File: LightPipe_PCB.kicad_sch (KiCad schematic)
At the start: 12 parts, among them X1 Lumberg KLB4, X2 Lumberg KLB4, X3 XT30, X4.1 Cable-0.7mm, X4.2 Cable-0.7mm, X5.1 Cable-1.5mm, X5.2 Cable-1.5mm

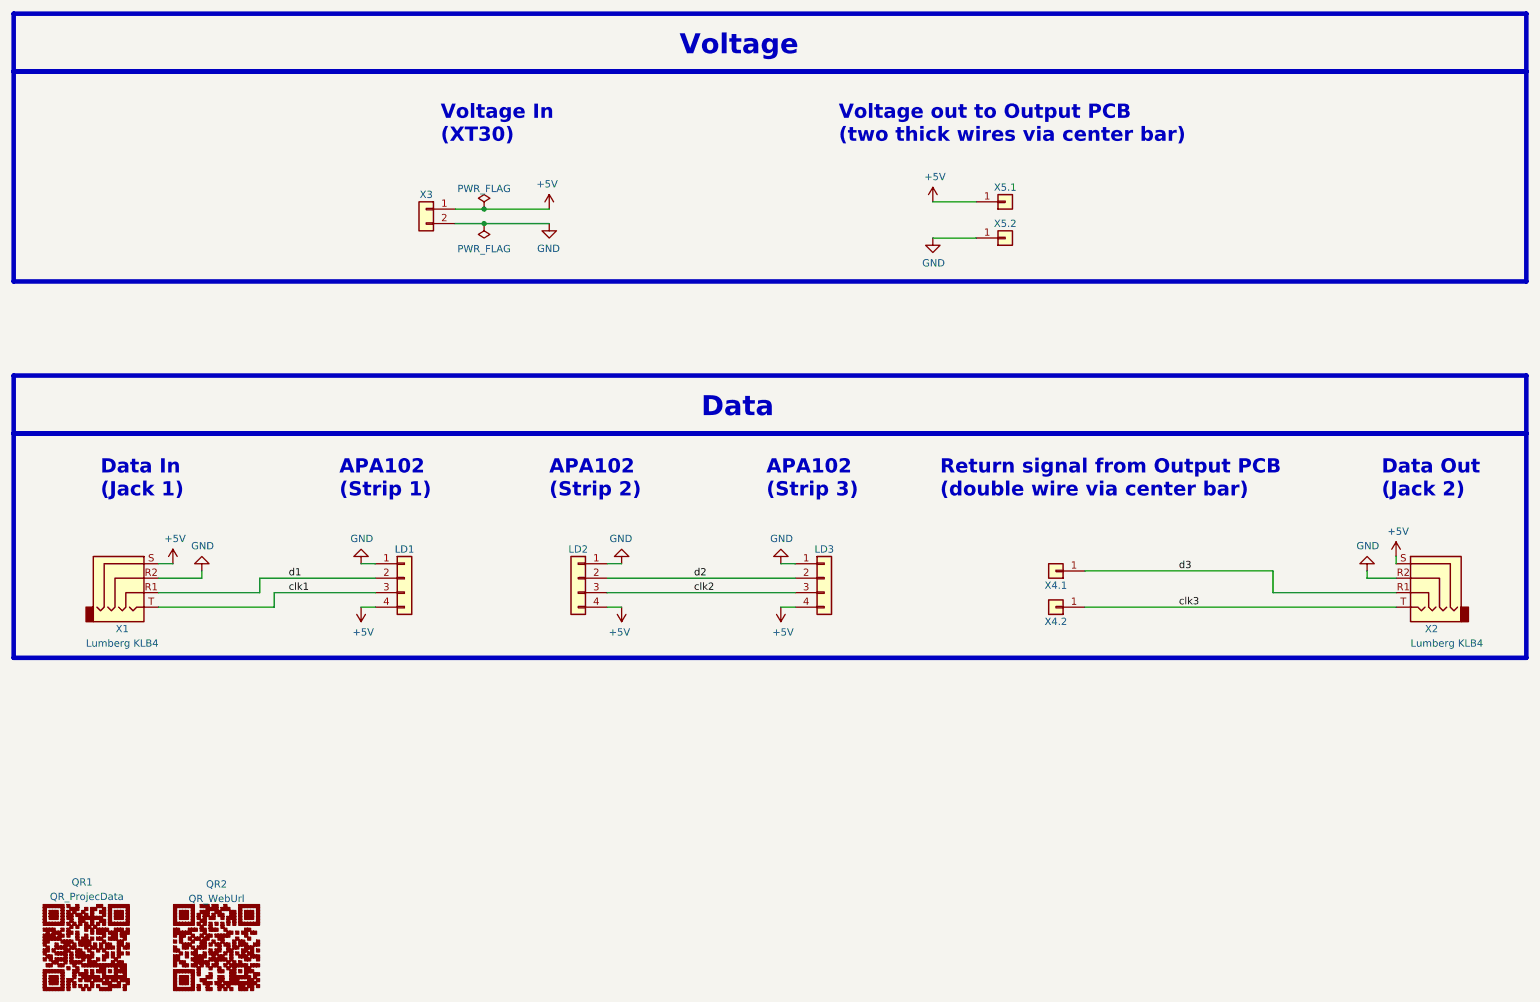
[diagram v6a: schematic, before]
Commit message: Optimize PCB for more common LED-Strip (GND, D, CLK, 5V) → It could be a good idea to change X4.1, X4.2, X5.1 and X5.2 to a standard footprint. There is always trouble with this custom footprints.
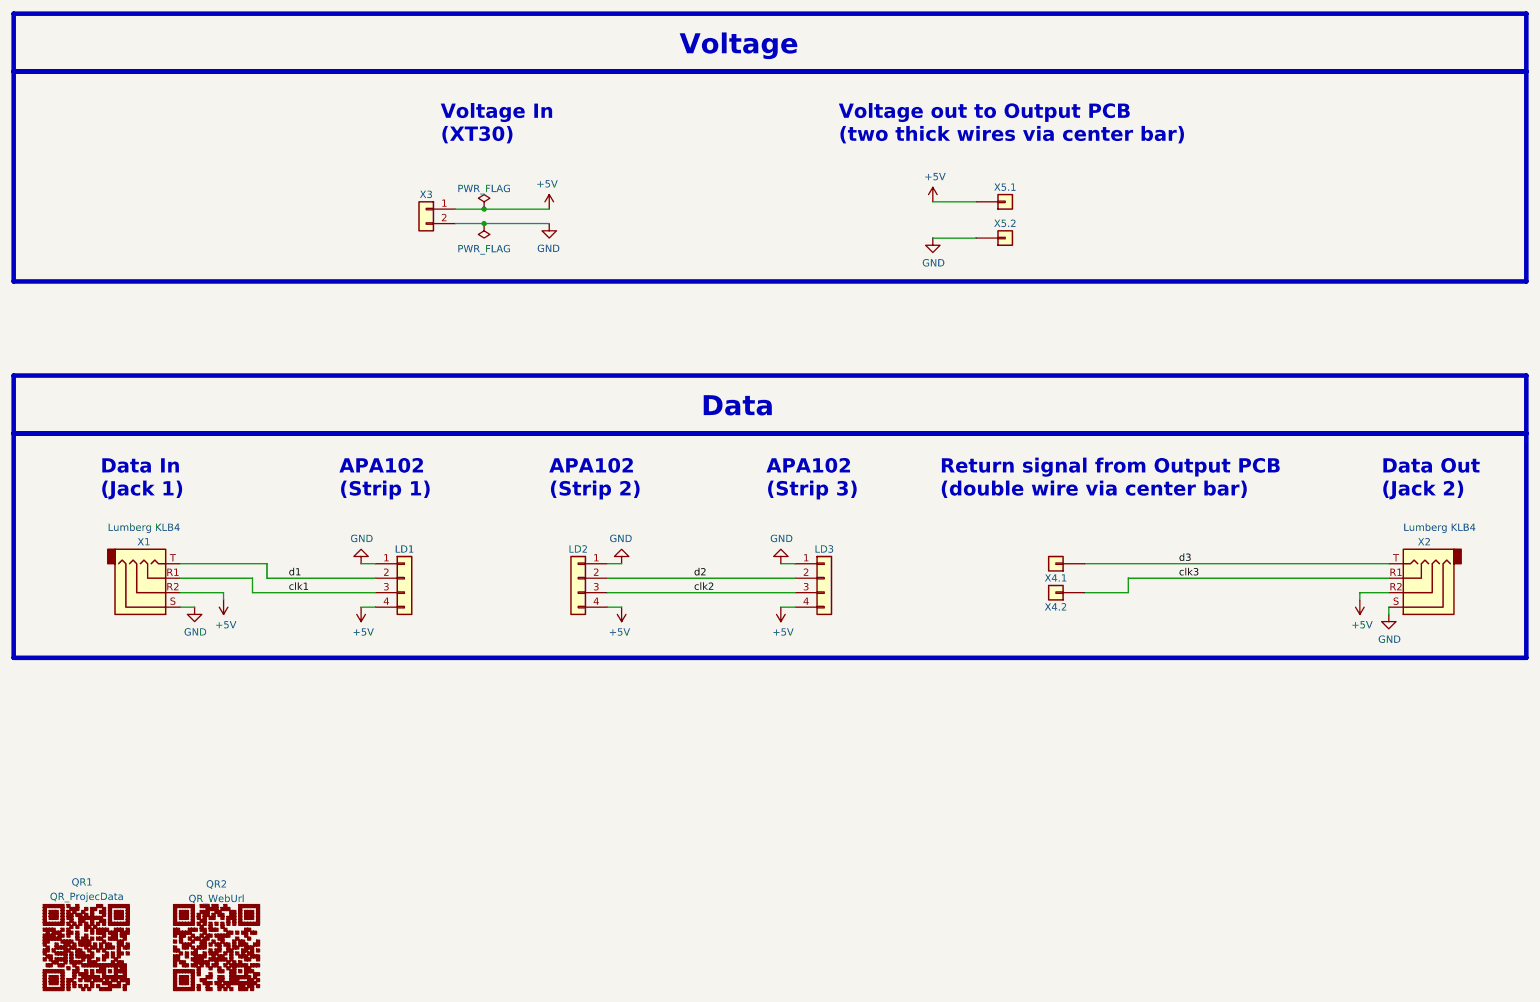
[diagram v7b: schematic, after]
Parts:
- removed X5.1: Cable-1.5mm, h8-Connectors:Solder-Pad-THT-1.5mm, symbol Connector_Generic:Conn_01x01
- added X5.2: Cable-1.5mm, h8-Connectors:Solder-Pad-THT-1.5mm, symbol Connector_Generic:Conn_01x01
- LD1, LD2, LD3, X4.1, X4.2: now left out of the parts list
- X5.1: renamed from X5.2; now left out of the parts list
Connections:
- net +5V: now also X1.R2, X2.R2, X5.1.1 (Pin_1); no longer X1.S, X2.S
- net GND: now also X1.S, X2.S, X5.2.1 (Pin_1); no longer X1.R2, X2.R2, X5.1.1 (Pin_1)
- net clk1: now also X1.R1; no longer X1.T
- net clk3: now also X2.R1; no longer X2.T
- net d1: now also X1.T; no longer X1.R1
- net d3: now also X2.T; no longer X2.R1
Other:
- moved on the sheet: X1, X2

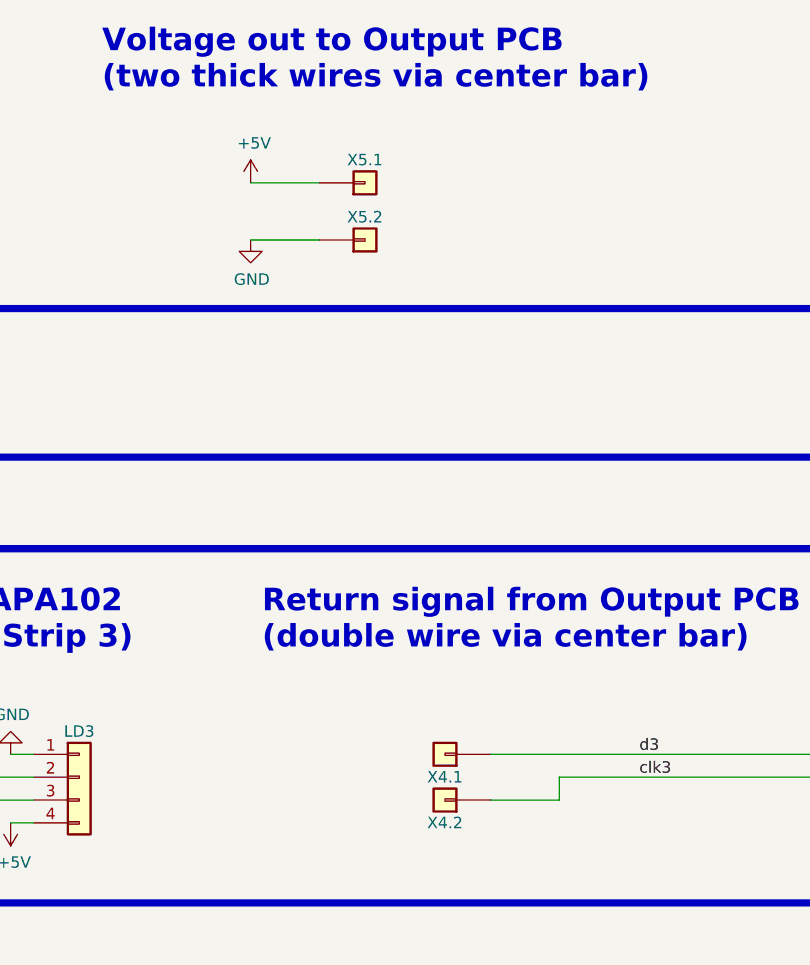
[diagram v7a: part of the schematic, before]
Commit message: Try to run KiBot - but it does not work well with KiCad 7.0 → Downgrade to KiCad 6.0?
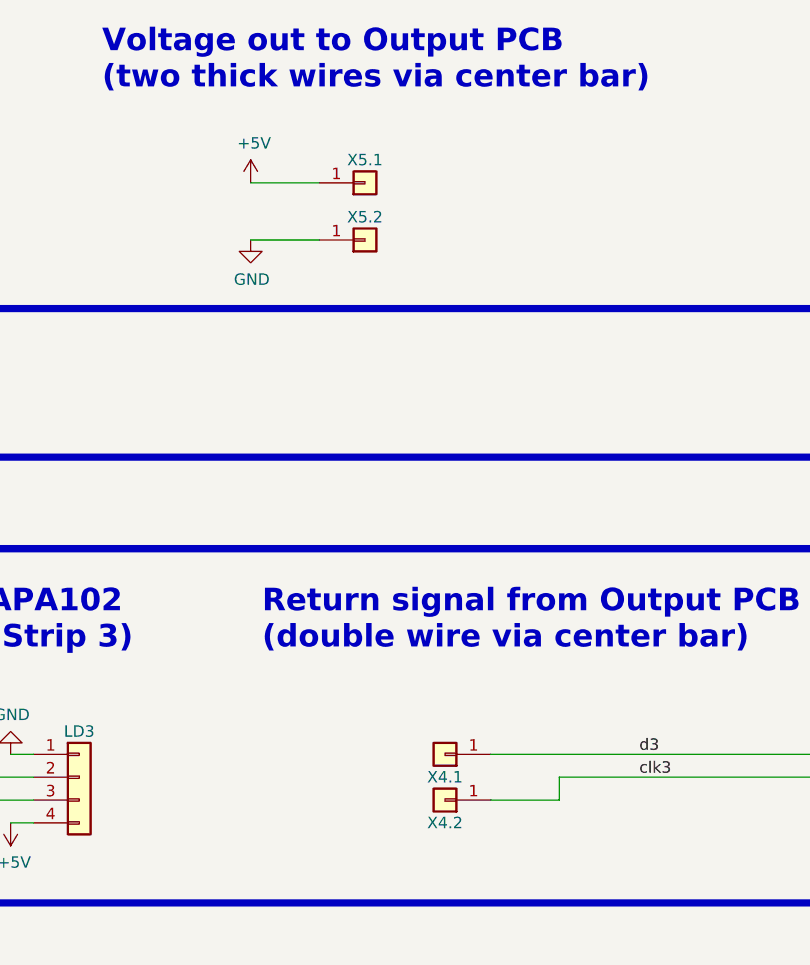
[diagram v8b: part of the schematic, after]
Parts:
- X3: LCSC C108769 -> (none); LCSC# (none) -> C108769; MF Changzhou Amass Elec -> Changzhou Amass Elec
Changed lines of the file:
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@@
       (effects (font (size 1.27 1.27)) hide)
     )
-    (property "MF" "Changzhou Amass Elec " (at 87.63 54.61 0)
+    (property "MF" "Changzhou Amass Elec" (at 87.63 54.61 0)
       (effects (font (size 1.27 1.27)) hide)
     )
@@
       (effects (font (size 1.27 1.27)) hide)
     )
-    (property "LCSC" "C108769" (at 87.63 54.61 0)
+    (property "LCSC#" "C108769" (at 87.63 54.61 0)
       (effects (font (size 1.27 1.27)) hide)
     )
@@
     )
   )
-  (symbol (lib_name "Conn_01x01_3") (lib_id "Connector_Generic:Conn_01x01") (at 189.23 53.34 0) (mirror x) (unit 1)
+  (symbol (lib_id "Connector_Generic:Conn_01x01") (at 189.23 53.34 0) (mirror x) (unit 1)
     (in_bom no) (on_board yes) (dnp no)
     (property "Reference" "X5.1" (at 189.23 50.8 0)
@@
     )
   )
-  (symbol (lib_name "Conn_01x01_1") (lib_id "Connector_Generic:Conn_01x01") (at 198.12 116.84 180) (unit 1)
+  (symbol (lib_id "Connector_Generic:Conn_01x01") (at 198.12 116.84 180) (unit 1)
     (in_bom no) (on_board yes) (dnp no)
     (property "Reference" "X4.1" (at 198.12 119.38 0)
@@
     )
   )
-  (symbol (lib_name "Conn_01x01_3") (lib_id "Connector_Generic:Conn_01x01") (at 189.23 59.69 0) (mirror x) (unit 1)
+  (symbol (lib_id "Connector_Generic:Conn_01x01") (at 189.23 59.69 0) (mirror x) (unit 1)
     (in_bom no) (on_board yes) (dnp no)
     (property "Reference" "X5.2" (at 189.23 57.15 0)
@@
     )
   )
-  (symbol (lib_name "Conn_01x01_2") (lib_id "Connector_Generic:Conn_01x01") (at 198.12 121.92 180) (unit 1)
+  (symbol (lib_id "Connector_Generic:Conn_01x01") (at 198.12 121.92 180) (unit 1)
     (in_bom no) (on_board yes) (dnp no)
     (property "Reference" "X4.2" (at 198.12 124.46 0)
